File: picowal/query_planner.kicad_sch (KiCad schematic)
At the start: 23 parts, among them J1 Upstream, J2 Downstream, J3 UART_DBG, J4 SWD_QRY, J5 RJ45, J6 SWD_IDX, U1 iCE40HX8K-CT256, U10 AP2112K-1.2, U11 RP2354B_IDX, U12 LY68L6400_IDX, U13 W5500, U14 W25Q128_IDX, U15 TPS62A01_IDX, U2 RP2354B, U3 IS61WV25616BLL, U4 IS61WV25616BLL, U5 LY68L6400_8MB, U6 W25Q128JVSIQ, U7 W25Q32JVSIQ, U8 TPS62A01, U9 AP2112K-3.3, Y1 12MHz, Y2 25MHz

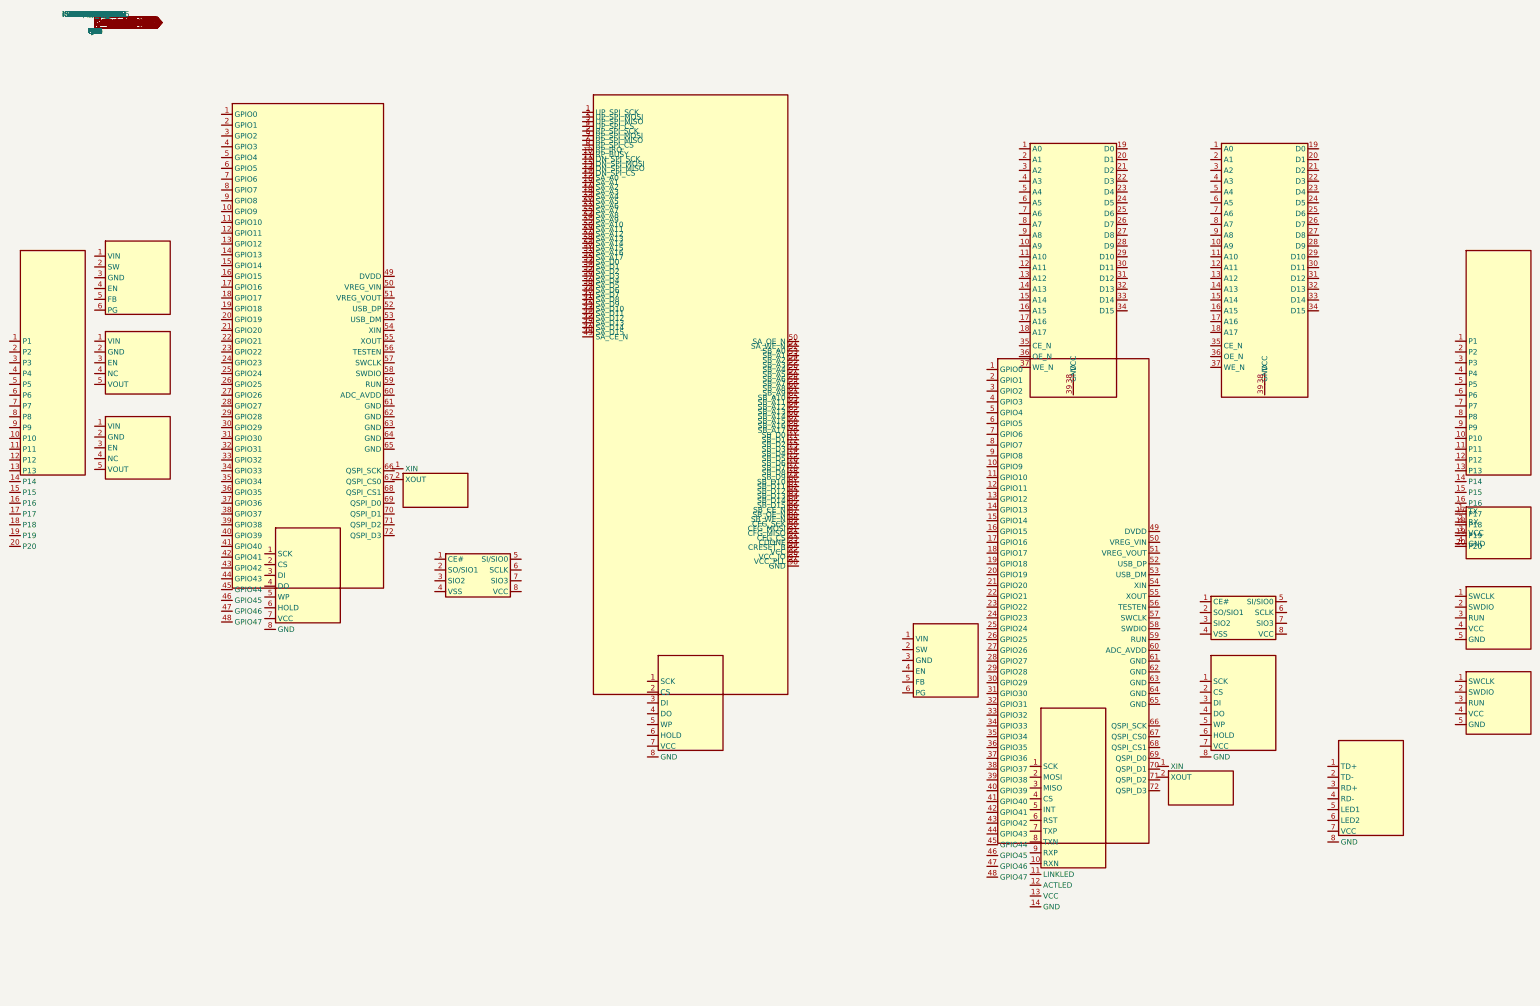
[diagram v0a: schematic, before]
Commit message: Upgrade PicoWAL: iCE40HX8K → ECP5-5G-45F + 3× NVMe M.2 RAID
Swap FPGA to LFE5UM5G-45F (CABGA381) for 4× 3.125Gbps SerDes.
3 SerDes channels → PCIe Gen1 x1 → M.2 M-key NVMe drives (RAID).
4th SerDes spare for future upstream PCIe or inter-card link.

New components:
  - 3× M.2 M-key NVMe connectors (J7/J8/J9)
  - 100MHz LVDS differential oscillator (PCIe refclk)
  - TPS54331 3A buck for NVMe 3.3V power rail
  - TPS62A02 buck for ECP5 1.1V core (replaces AP2112K-1.2 LDO)
  - W25Q128 replaces W25Q32 for ECP5 config (45F bitstream is larger)

Board: 100×55mm → 130×80mm to accommodate M.2 slots.
BOM: £31.90 → £48.60 (excl. NVMe SSDs).
Pin budget: 110/205 I/O + 3/4 SerDes channels used.
Power: 2.8W board logic + ~10W for 3× NVMe drives.
RTL tests: 15/15 PASS (comment-only changes in query_bypass.v).

Co-authored-by: Copilot <223556219+Copilot@users.noreply.github.com>
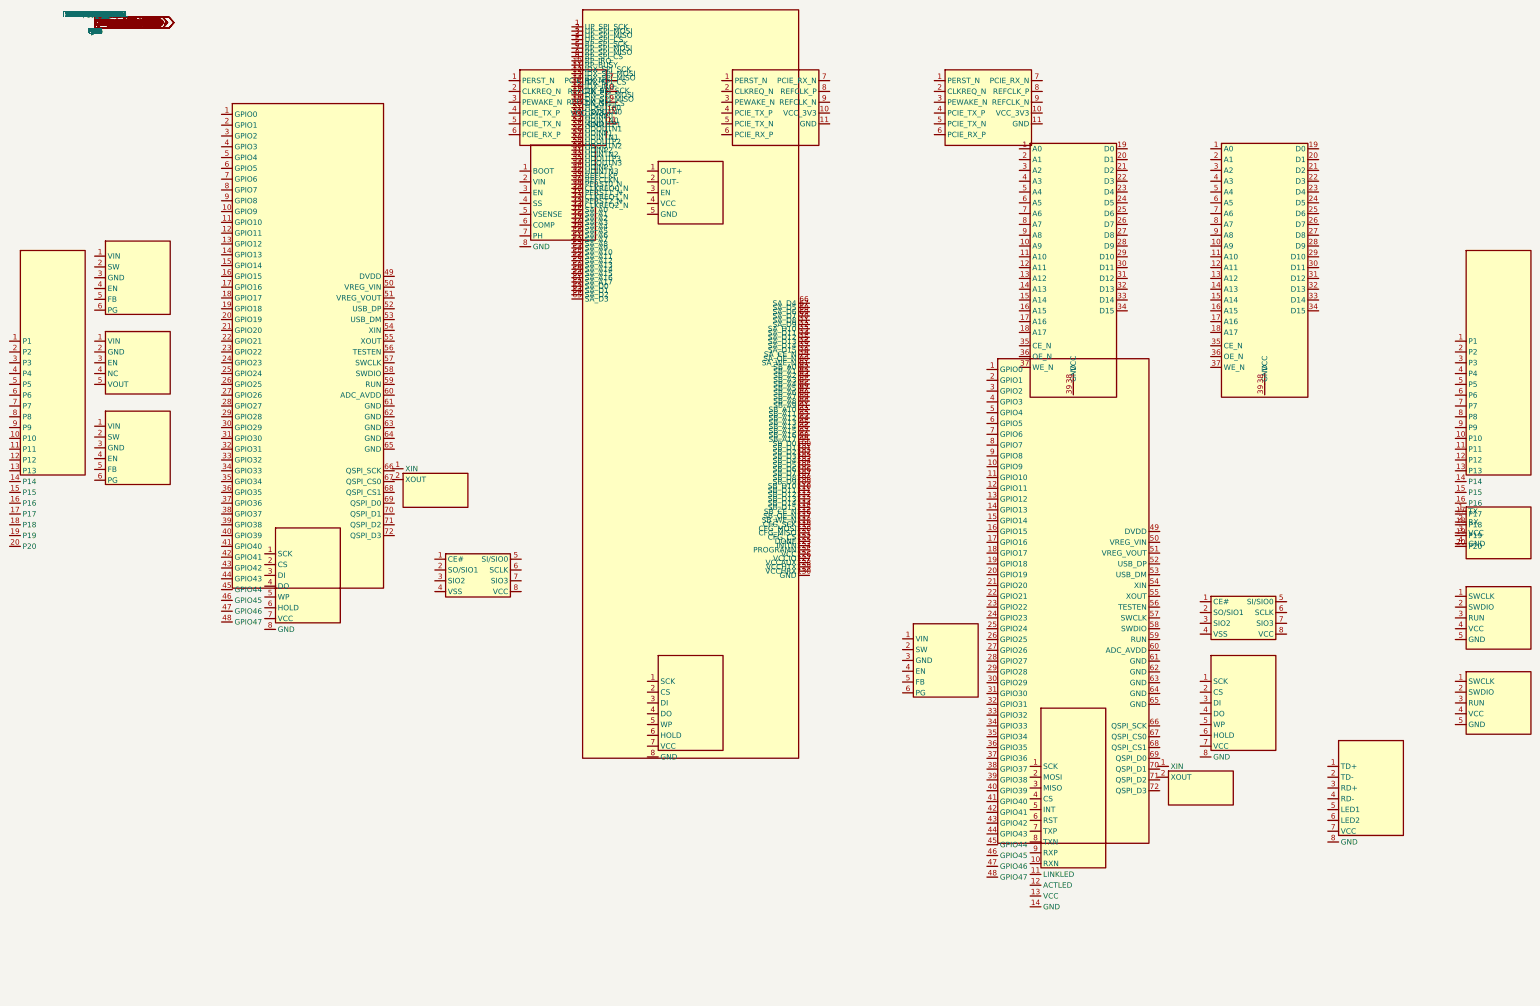
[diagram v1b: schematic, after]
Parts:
- removed U1: iCE40HX8K-CT256, symbol ice40hx8k_ct256
- removed U10: AP2112K-1.2, symbol ap2112k_1_2
- removed U7: W25Q32JVSIQ, symbol w25q32jvsiq
- added J7: NVMe_0, symbol m2_mkey_nvme
- added J8: NVMe_1, symbol m2_mkey_nvme
- added J9: NVMe_2, symbol m2_mkey_nvme
- added U1: LFE5UM5G-45F, symbol ecp5_5g_45f
- added U10: TPS62A02_CORE, symbol tps62a02
- added U16: TPS54331_NVMe, symbol tps54331
- added U7: W25Q128_CFG, symbol w25q128jvsiq
- added Y3: 100MHz_DIFF, symbol 100mhz_diff
- U8: value TPS62A01 -> TPS62A01_QRY
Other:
- title: PicoWAL Query Planner v1.0 -> PicoWAL Query Processor v1.0 — ECP5-5G + 3× NVMe RAID

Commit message: Add deterministic 8-bit parallel bus, swap SPI for pico interfaces
- New RTL: fpga_pico_bus.v — 8-bit bidirectional bus with RDY/ACK handshake
  - DATA[7:0] + RDY + ACK + DIR + SOF + EOF + SOCK[1:0] = 15 pins/pico
  - TX FIFO (512 bytes), ACK synchronizer (3-stage CDC)
  - Timeout recovery, direction turnaround dead cycle
  - ~50 MB/s @ 50MHz, PIO+DMA friendly on pico side

- Deterministic architecture:
  - Pico A (QRY): owns TCP streams, parses queries, streams results
  - Pico B (IDX): owns all writes, WAL, index maintenance (no contention)
  - Direct reads: FPGA -> NVMe -> TCP (zero pico, deterministic pipeline)
  - Drive 0,1 = data shards, Drive 2 = WAL + indexes (pico B exclusive)

- Generator updated: SPI register map -> 8-bit parallel bus pins
  - Pin budget: 133/205 (was 114/205 with SPI — +19 pins, still comfortable)
  - ECP5 symbol updated with QRY_D[0:7]/IDX_D[0:7] bus pins

- Testbench: tb_fpga_pico_bus.v — 12/12 PASS
  - TX single/multi-byte, timeout, RX, bidirectional, FIFO backpressure, reset

Co-authored-by: Copilot <223556219+Copilot@users.noreply.github.com>
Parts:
- removed J5: RJ45, symbol rj45_magjack
- removed U13: W5500, symbol w5500
- added J5: RJ45_PoE, symbol rj45_poe_magjack
- added U13: RTL8221B, symbol rtl8211f
- added U17: TPS23753A_PoE, symbol tps23753a
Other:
- title: PicoWAL Query Processor v1.0 — ECP5-5G + 3× NVMe RAID -> PicoWAL Query Processor v1.0 — ECP5-5G + 3× NVMe RAID + GbE TOE + PoE
